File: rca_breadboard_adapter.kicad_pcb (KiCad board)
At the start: 2 copper layers, 22.9 x 22.9 mm, 4 parts, among them J1 Conn_Coaxial, J2 Conn_Coaxial, J3 Conn_02x03_Odd_Even, J4 Conn_02x03_Odd_Even

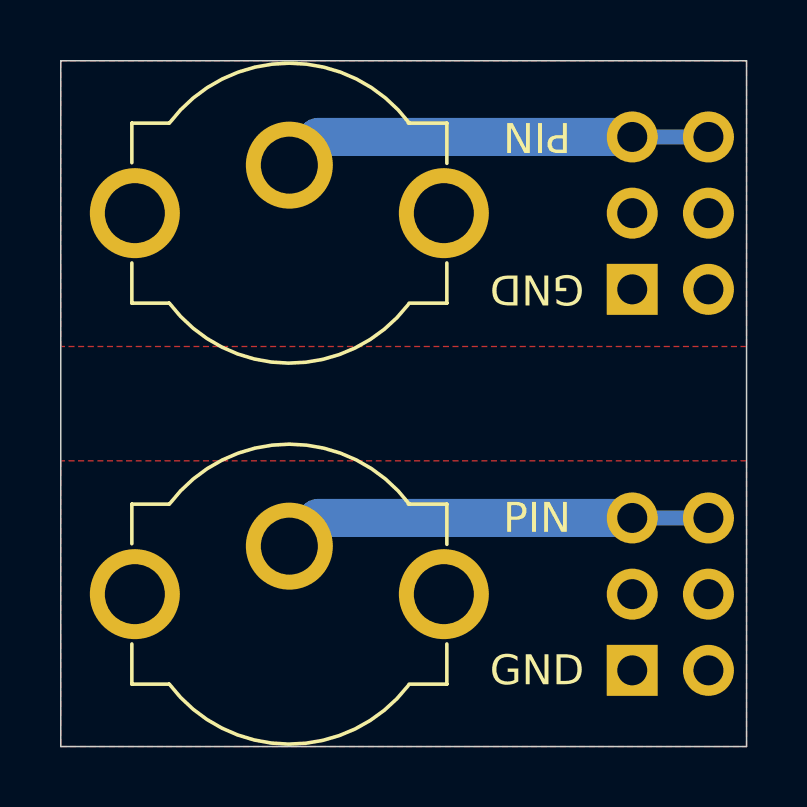
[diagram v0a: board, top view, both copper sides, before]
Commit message: Update silkscreen with github URL
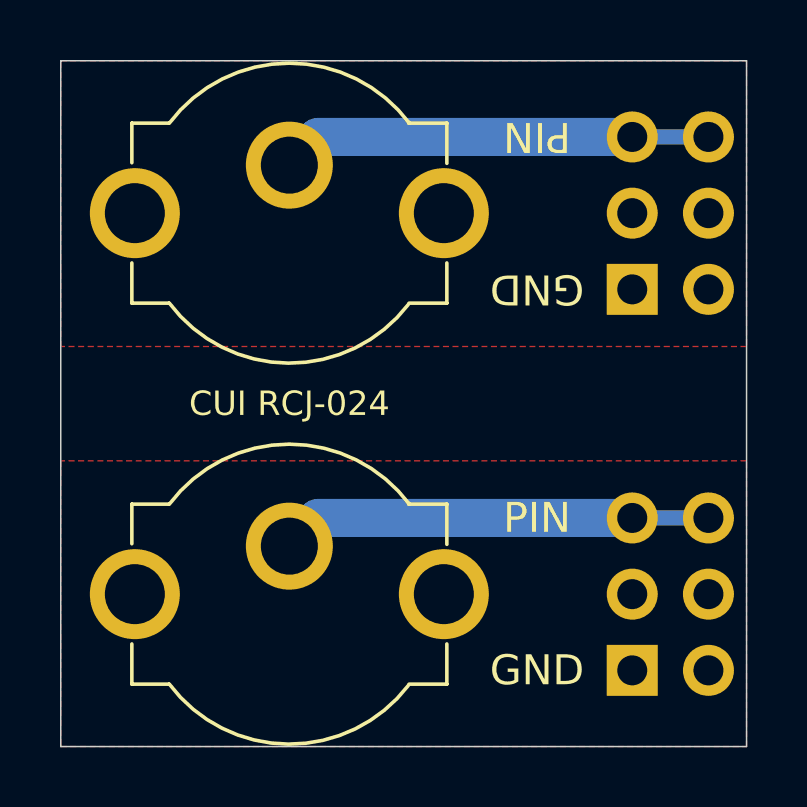
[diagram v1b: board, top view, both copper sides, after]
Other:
- board text added: "CUI RCJ-024"
- board text added: "RCA Breadboard Adapter v1"
- board text added: "github.com/joem"
- board text removed: "(use: CUI RCJ-02X)"
- board text removed: "RCA Breadboard Adapter v1 by JWM"
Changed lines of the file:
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@@
   (general
     (thickness 1.6002)
-    (drawings 10)
+    (drawings 11)
     (tracks 6)
     (zones 0)
@@
     (39 F.Mask user)
     (44 Edge.Cuts user)
-    (45 Margin user hide)
+    (45 Margin user)
     (46 B.CrtYd user hide)
     (47 F.CrtYd user hide)
@@
     )
   )
-  (gr_text "(use: CUI RCJ-02X)" (at 148.59 55.245 180) (layer B.SilkS)
+  (gr_text github.com/joem (at 147.955 56.515 180) (layer B.SilkS)
     (effects (font (size 1 1) (thickness 0.15)) (justify mirror))
+  )
+  (gr_text "CUI RCJ-024" (at 147.32 58.42) (layer F.SilkS)
+    (effects (font (size 0.8128 0.8128) (thickness 0.1524)))
   )
   (gr_line (start 162.56 46.99) (end 139.7 46.99) (layer Edge.Cuts) (width 0.05))
   (gr_line (start 162.56 69.85) (end 139.7 69.85) (layer Edge.Cuts) (width 0.05))
   (gr_line (start 162.56 46.99) (end 162.56 69.85) (layer Edge.Cuts) (width 0.05))
-  (gr_text "RCA Breadboard Adapter v1\nby JWM" (at 151.13 58.42 180) (layer B.SilkS)
+  (gr_text "RCA Breadboard Adapter v1" (at 151.13 58.42 180) (layer B.SilkS)
     (effects (font (size 1 1) (thickness 0.15)) (justify mirror))
   )

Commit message: Update project to kicad 6+
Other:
- net class Default removed
